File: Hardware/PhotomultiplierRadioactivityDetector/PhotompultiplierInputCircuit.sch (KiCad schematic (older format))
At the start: 40 parts, among them J10 Conn_01x01_Male, J11 Conn_01x01_Male, J12 Conn_01x01_Male, J13 Conn_01x01_Male, J14 Conn_01x01_Male, J3 Conn_01x01_Male, J4 Conn_01x01_Male, J5 Conn_01x01_Male, J6 Conn_01x01_Male, J7 Conn_01x01_Male, J8 Conn_01x01_Male, J9 Conn_01x01_Male

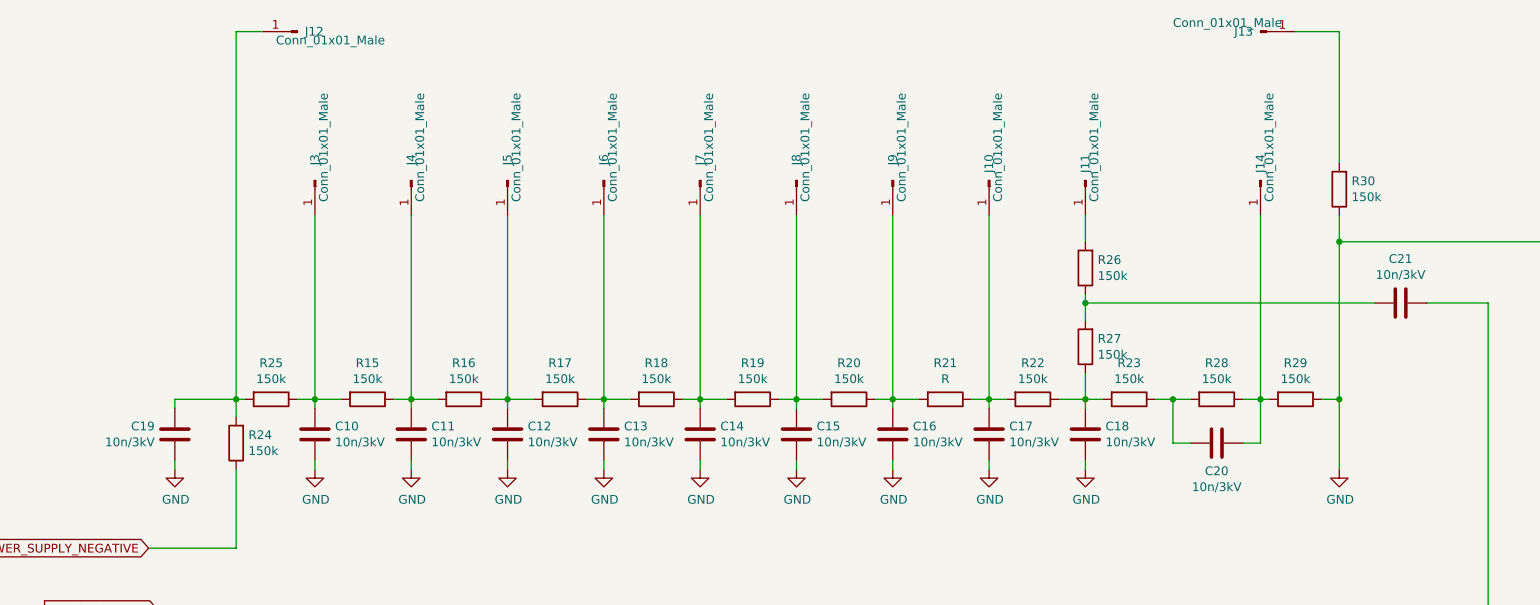
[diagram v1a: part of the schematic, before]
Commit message: draft of hw power supply
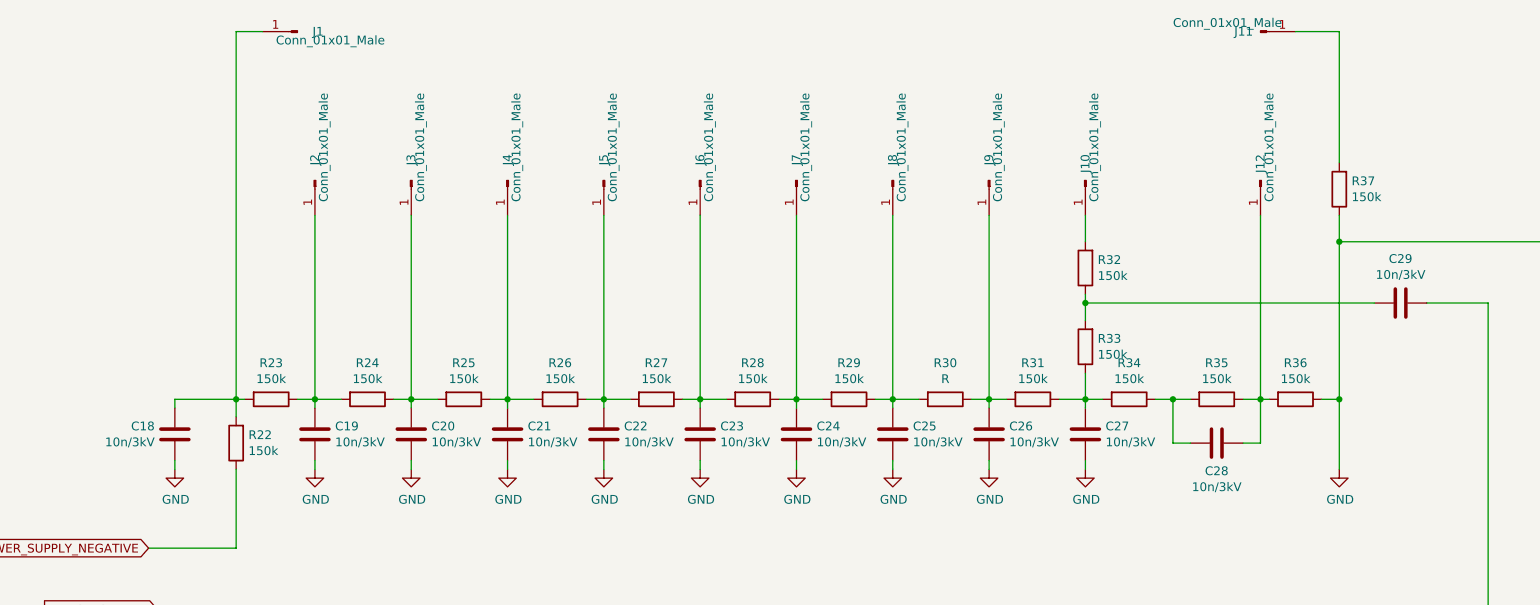
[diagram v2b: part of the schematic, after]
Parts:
- renumbered C19 to C18, C10 to C19, C11 to C20, C12 to C21, C13 to C22, C14 to C23, C15 to C24, C16 to C25, C17 to C26, C18 to C27, C20 to C28, C21 to C29, J12 to J1, J11 to J10, J13 to J11, J14 to J12, J3 to J2, J4 to J3, J5 to J4, J6 to J5, J7 to J6, J8 to J7, J9 to J8, J10 to J9, R24 to R22, R25 to R23, R15 to R24, R16 to R25, R17 to R26, R18 to R27, R19 to R28, R20 to R29, R21 to R30, R22 to R31, R26 to R32, R27 to R33, R23 to R34, R28 to R35, R29 to R36, R30 to R37

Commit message: add element/footprint for photomultiplier
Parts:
- removed J1, J10, J11, J12, J2, J3, J4, J5, J6, J7, J8, J9: Conn_01x01_Male, Connector_Pin:Pin_D1.1mm_L10.2mm_W3.5mm_Flat, symbol Connector:Conn_01x01_Male
- added EL1: Photomultiplier, PhotomultiplierRadioactivityDetector:PhotomultiplierGeneric, symbol PhotomultiplierRadioactivityDetector:Photomultiplier
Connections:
- net at C19.1, R23.1, R24.2: now also EL1.2
- net at C18.1, R22.2, R23.2: now also EL1.1
- net at C28.1, R35.1, R36.2: now also EL1.11
- net at R37.2: now also EL1.12
- net at R32.2: now also EL1.10
- net at C20.1, R24.1, R25.2: now also EL1.3
- net at C21.1, R25.1, R26.2: now also EL1.4
- net at C22.1, R26.1, R27.2: now also EL1.5
- net at C23.1, R27.1, R28.2: now also EL1.6
- net at C24.1, R28.1, R29.2: now also EL1.7
- net at C25.1, R29.1, R30.2: now also EL1.8
- net at C26.1, R30.1, R31.2: now also EL1.9
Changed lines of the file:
@@
 $EndDescr
-$Comp
-L Connector:Conn_01x01_Male J2
-U 1 1 5EDAB7C9
-P 3050 2450
-F 0 "J2" H 2900 2450 50  0000 L CNN
-F 1 "Conn_01x01_Male" H 2550 2500 50  0000 L CNN
-F 2 "Connector_Pin:Pin_D1.1mm_L10.2mm_W3.5mm_Flat" H 3050 2450 50  0001 C CNN
-F 3 "~" H 3050 2450 50  0001 C CNN
-	1    3050 2450
-	0    1    1    0
-$EndComp
 $Comp
 L Device:R R24
@@
 	3050 4100 3050 4050
 Wire Wire Line
-	3050 2650 3050 3700
-Wire Wire Line
 	3200 3700 3050 3700
 Connection ~ 3050 3700
@@
 Wire Wire Line
 	3050 3700 2950 3700
-$Comp
-L Connector:Conn_01x01_Male J3
-U 1 1 5EDAB7E7
-P 3600 2450
-F 0 "J3" H 3450 2450 50  0000 L CNN
-F 1 "Conn_01x01_Male" H 3100 2500 50  0000 L CNN
-F 2 "Connector_Pin:Pin_D1.1mm_L10.2mm_W3.5mm_Flat" H 3600 2450 50  0001 C CNN
-F 3 "~" H 3600 2450 50  0001 C CNN
-	1    3600 2450
-	0    1    1    0
-$EndComp
 $Comp
 L Device:R R25
@@
 	3600 4100 3600 4050
 Wire Wire Line
-	3600 2650 3600 3700
-Wire Wire Line
 	3750 3700 3600 3700
 Connection ~ 3600 3700
@@
 Wire Wire Line
 	3600 3700 3500 3700
-$Comp
-L Connector:Conn_01x01_Male J4
-U 1 1 5EDAB805
-P 4150 2450
-F 0 "J4" H 4000 2450 50  0000 L CNN
-F 1 "Conn_01x01_Male" H 3650 2500 50  0000 L CNN
-F 2 "Connector_Pin:Pin_D1.1mm_L10.2mm_W3.5mm_Flat" H 4150 2450 50  0001 C CNN
-F 3 "~" H 4150 2450 50  0001 C CNN
-	1    4150 2450
-	0    1    1    0
-$EndComp
 $Comp
 L Device:R R26
@@
 	4150 4100 4150 4050
 Wire Wire Line
-	4150 2650 4150 3700
-Wire Wire Line
 	4300 3700 4150 3700
 Connection ~ 4150 3700
@@
 Wire Wire Line
 	4150 3700 4050 3700
-$Comp
-L Connector:Conn_01x01_Male J5
-U 1 1 5EDAB823
-P 4700 2450
-F 0 "J5" H 4550 2450 50  0000 L CNN
-F 1 "Conn_01x01_Male" H 4200 2500 50  0000 L CNN
-F 2 "Connector_Pin:Pin_D1.1mm_L10.2mm_W3.5mm_Flat" H 4700 2450 50  0001 C CNN
-F 3 "~" H 4700 2450 50  0001 C CNN
-	1    4700 2450
-	0    1    1    0
-$EndComp
 $Comp
 L Device:R R27
@@
 	4700 4100 4700 4050
 Wire Wire Line
-	4700 2650 4700 3700
-Wire Wire Line
 	4850 3700 4700 3700
 Connection ~ 4700 3700
@@
 Wire Wire Line
 	4700 3700 4600 3700
-$Comp
-L Connector:Conn_01x01_Male J6
-U 1 1 5EDAB841
-P 5250 2450
-F 0 "J6" H 5100 2450 50  0000 L CNN
-F 1 "Conn_01x01_Male" H 4750 2500 50  0000 L CNN
-F 2 "Connector_Pin:Pin_D1.1mm_L10.2mm_W3.5mm_Flat" H 5250 2450 50  0001 C CNN
-F 3 "~" H 5250 2450 50  0001 C CNN
-	1    5250 2450
-	0    1    1    0
-$EndComp
 $Comp
 L Device:R R28
@@
 	5250 3700 5150 3700
 $Comp
-L Connector:Conn_01x01_Male J7
-U 1 1 5EDAB85F
-P 5800 2450
-F 0 "J7" H 5650 2450 50  0000 L CNN
-F 1 "Conn_01x01_Male" H 5300 2500 50  0000 L CNN
-F 2 "Connector_Pin:Pin_D1.1mm_L10.2mm_W3.5mm_Flat" H 5800 2450 50  0001 C CNN
-F 3 "~" H 5800 2450 50  0001 C CNN
-	1    5800 2450
-	0    1    1    0
-$EndComp
-$Comp
 L Device:R R29
 U 1 1 5EDAB865
@@
 	5800 3700 5700 3700
 $Comp
-L Connector:Conn_01x01_Male J8
-U 1 1 5EDAB87D
-P 6350 2450
-F 0 "J8" H 6200 2450 50  0000 L CNN
-F 1 "Conn_01x01_Male" H 5850 2500 50  0000 L CNN
-F 2 "Connector_Pin:Pin_D1.1mm_L10.2mm_W3.5mm_Flat" H 6350 2450 50  0001 C CNN
-F 3 "~" H 6350 2450 50  0001 C CNN
-	1    6350 2450
-	0    1    1    0
-$EndComp
-$Comp
 L Device:R R30
 U 1 1 5EDAB883
@@
 	6350 4100 6350 4050
 Wire Wire Line
-	6350 2650 6350 3700
-Wire Wire Line
 	6500 3700 6350 3700
 Connection ~ 6350 3700
@@
 Wire Wire Line
 	6350 3700 6250 3700
-$Comp
-L Connector:Conn_01x01_Male J9
-U 1 1 5EDAB89B
-P 6900 2450
-F 0 "J9" H 6750 2450 50  0000 L CNN
-F 1 "Conn_01x01_Male" H 6400 2500 50  0000 L CNN
-F 2 "Connector_Pin:Pin_D1.1mm_L10.2mm_W3.5mm_Flat" H 6900 2450 50  0001 C CNN
-F 3 "~" H 6900 2450 50  0001 C CNN
-	1    6900 2450
-	0    1    1    0
-$EndComp
 $Comp
 L Device:R R31
@@
 	6900 4100 6900 4050
 Wire Wire Line
-	6900 2650 6900 3700
-Wire Wire Line
 	7000 3700 6900 3700
 Connection ~ 6900 3700
@@
 Wire Wire Line
 	6900 3700 6800 3700
-$Comp
-L Connector:Conn_01x01_Male J10
-U 1 1 5EDAB8B9
-P 7450 2450
-F 0 "J10" H 7300 2450 50  0000 L CNN
-F 1 "Conn_01x01_Male" H 6950 2500 50  0000 L CNN
-F 2 "Connector_Pin:Pin_D1.1mm_L10.2mm_W3.5mm_Flat" H 7450 2450 50  0001 C CNN
-F 3 "~" H 7450 2450 50  0001 C CNN
-	1    7450 2450
-	0    1    1    0
-$EndComp
 $Comp
 L Device:R R34
@@
 Text GLabel 2100 4550 0    50   Input ~ 0
 TUBE_POWER_SUPPLY_NEGATIVE
-Wire Wire Line
-	2600 3700 2600 1600
-Wire Wire Line
-	2600 1600 2750 1600
-$Comp
-L Connector:Conn_01x01_Male J1
-U 1 1 5ED7B685
-P 2950 1600
-F 0 "J1" H 2800 1600 50  0000 L CNN
-F 1 "Conn_01x01_Male" H 2450 1650 50  0000 L CNN
-F 2 "Connector_Pin:Pin_D1.1mm_L10.2mm_W3.5mm_Flat" H 2950 1600 50  0001 C CNN
-F 3 "~" H 2950 1600 50  0001 C CNN
-	1    2950 1600
-	-1   0    0    1
-$EndComp
 $Comp
 L Device:R R35
@@
 Wire Wire Line
 	8450 3700 8500 3700
-$Comp
-L Connector:Conn_01x01_Male J12
-U 1 1 5ED81517
-P 8450 2450
-F 0 "J12" H 8300 2450 50  0000 L CNN
-F 1 "Conn_01x01_Male" H 7950 2500 50  0000 L CNN
-F 2 "Connector_Pin:Pin_D1.1mm_L10.2mm_W3.5mm_Flat" H 8450 2450 50  0001 C CNN
-F 3 "~" H 8450 2450 50  0001 C CNN
-	1    8450 2450
-	0    1    1    0
-$EndComp
-Wire Wire Line
-	8450 2650 8450 3700
 Wire Bus Line
 	11200 2550 11200 2600
-$Comp
-L Connector:Conn_01x01_Male J11
-U 1 1 5ED82C8D
-P 8450 1600
-F 0 "J11" H 8300 1600 50  0000 L CNN
-F 1 "Conn_01x01_Male" H 7950 1650 50  0000 L CNN
-F 2 "Connector_Pin:Pin_D1.1mm_L10.2mm_W3.5mm_Flat" H 8450 1600 50  0001 C CNN
-F 3 "~" H 8450 1600 50  0001 C CNN
-	1    8450 1600
-	1    0    0    -1
-$EndComp
 $Comp
 L power:GND #PWR044
@@
 Wire Wire Line
 	8900 3700 8900 2800
-Wire Wire Line
-	8650 1600 8900 1600
-Wire Wire Line
-	8900 1600 8900 2350
 $Comp
 L Device:R R33
@@
 	7450 3150 7450 3100
 Wire Wire Line
-	7450 2800 7450 2650
-Wire Wire Line
 	8900 2800 10100 2800
 Wire Wire Line
@@
 	1    0    0    -1
 $EndComp
+$Comp
+L PhotomultiplierRadioactivityDetector:Photomultiplier EL1
+U 1 1 5EE61F2A
+P 5450 1300
+F 0 "EL1" H 5525 1615 50  0000 C CNN
+F 1 "Photomultiplier" H 5525 1524 50  0000 C CNN
+F 2 "PhotomultiplierRadioactivityDetector:PhotomultiplierGeneric" H 5450 1550 50  0001 C CNN
+F 3 "" H 5450 1550 50  0001 C CNN
+	1    5450 1300
+	1    0    0    -1
+$EndComp
+Wire Wire Line
+	3050 1900 4850 1900
+Wire Wire Line
+	4850 1900 4850 1550
+Wire Wire Line
+	3050 1900 3050 3700
+Wire Wire Line
+	3600 2100 5000 2100
+Wire Wire Line
+	5000 2100 5000 1550
+Wire Wire Line
+	3600 2100 3600 3700
+Wire Wire Line
+	4150 2250 5150 2250
+Wire Wire Line
+	5150 2250 5150 1550
+Wire Wire Line
+	4150 2250 4150 3700
+Wire Wire Line
+	4700 2400 5300 2400
+Wire Wire Line
+	5300 2400 5300 1550
+Wire Wire Line
+	4700 2400 4700 3700
+Wire Wire Line
+	5450 2650 5450 1550
+Wire Wire Line
+	5250 2650 5450 2650
+Wire Wire Line
+	5600 2650 5600 1550
+Wire Wire Line
+	5600 2650 5800 2650
+Wire Wire Line
+	6350 2400 5750 2400
+Wire Wire Line
+	5750 2400 5750 1550
+Wire Wire Line
+	6350 2400 6350 3700
+Wire Wire Line
+	6900 2200 5900 2200
+Wire Wire Line
+	5900 2200 5900 1550
+Wire Wire Line
+	6900 2200 6900 3700
+Wire Wire Line
+	7450 2050 6050 2050
+Wire Wire Line
+	6050 2050 6050 1550
+Wire Wire Line
+	7450 2050 7450 2800
+Wire Wire Line
+	8450 1850 6200 1850
+Wire Wire Line
+	6200 1850 6200 1550
+Wire Wire Line
+	8450 1850 8450 3700
+Wire Wire Line
+	2600 1300 4600 1300
+Wire Wire Line
+	6450 1300 8900 1300
+Wire Wire Line
+	2600 1300 2600 3700
+Wire Wire Line
+	8900 1300 8900 2350
 $EndSCHEMATC

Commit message: draft of amplifier
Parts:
- added C33, C34: 10n/3kV, Capacitor_THT:C_Disc_D11.0mm_W5.0mm_P7.50mm, symbol Device:C
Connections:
- net DYNOE_OUTPUT: now also C20.2, R33.1; no longer C29.1
- net GND: now also C18.1, C25.1, EL1.12, R32.2, R33.2, C34.1; no longer C18.2, C19.2, C20.2, C21.2, C22.2, C23.2, C24.2, C25.2, C26.2, C27.2, R36.1
- net at EL1.2, R23.1, R24.2: now also C26.1, C27.2, R35.1; no longer C19.1
- net at EL1.1, R22.2, R23.2: now also C18.2, C21.2, C26.2, R34.1; no longer C18.1
- net at R37.2: now also EL1.11, R36.1; no longer EL1.12
- net at EL1.10: now also R31.1, R36.2, C33.1, C34.2; no longer R32.2
- net at EL1.3, R24.1, R25.2: now also C21.1, C22.2; no longer C20.1
- net at EL1.4, R25.1, R26.2: now also C27.1, C28.2; no longer C21.1
- net at C22.1, EL1.5, R26.1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: now also C23.2
- net at EL1.6, R27.1, R28.2: now also C28.1, C29.2; no longer C23.1
- net at EL1.7, R28.1, R29.2: now also C23.1, C24.2; no longer C24.1
- net at EL1.8, R29.1, R30.2: now also C29.1, C33.2; no longer C25.1
- net at EL1.9, R30.1, R31.2: now also C24.1, C25.2; no longer C26.1
- new net: C19.1, R34.2
- new net: C20.1, R35.2
- new net ANODE_OUTPUT: C19.2, R32.1
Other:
- moved on the sheet: C18, EL1, R22, R23, R24, R25, R26, R27, R28, R29, R30, R31

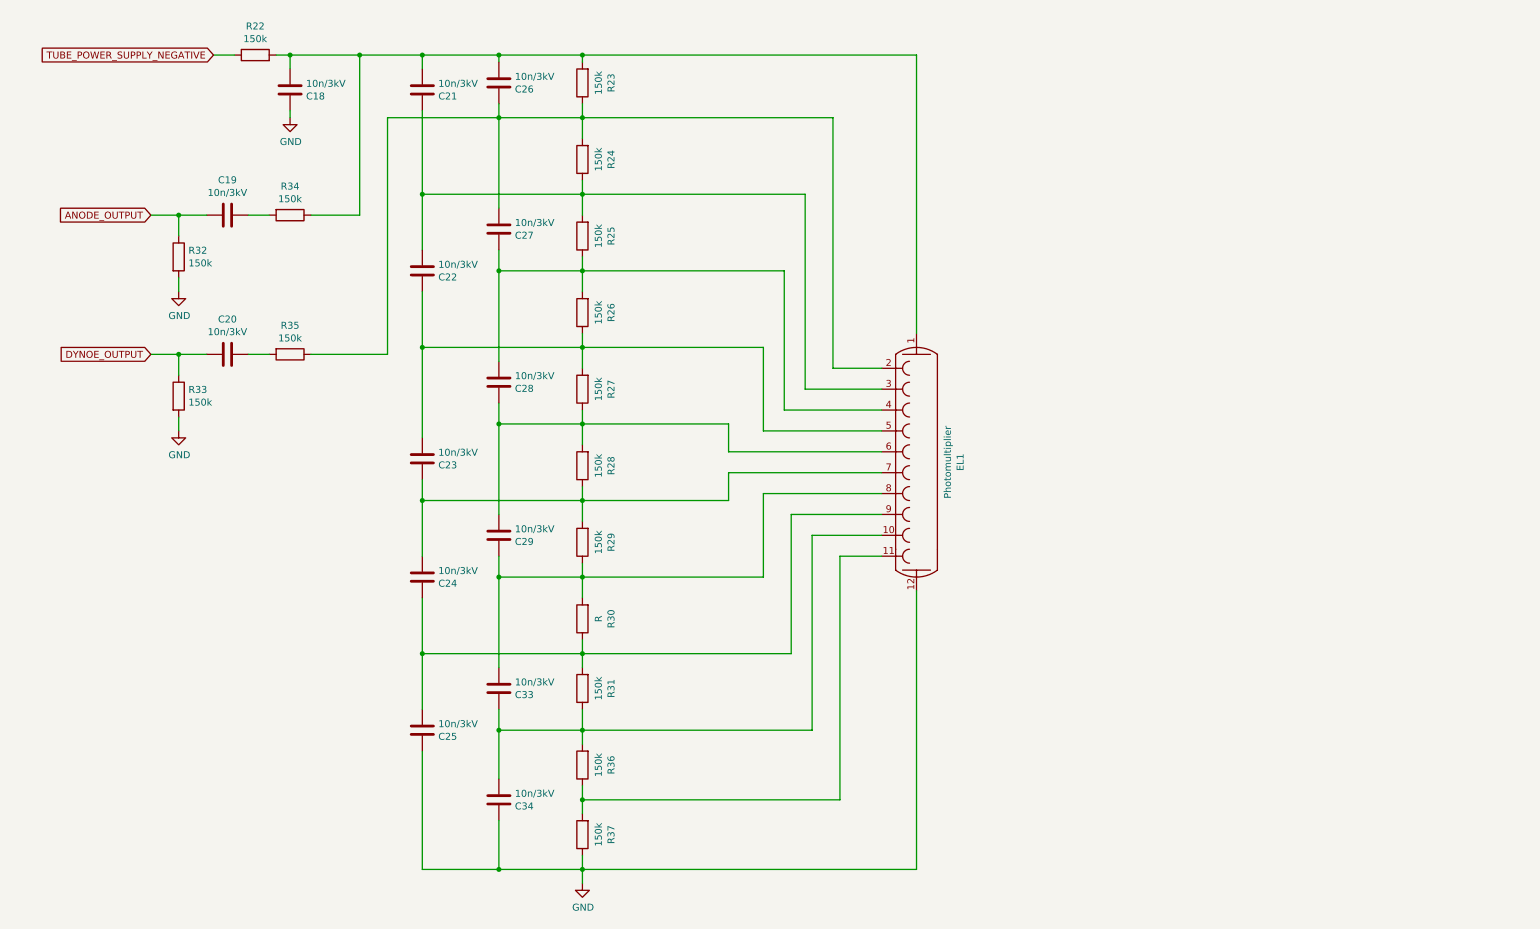
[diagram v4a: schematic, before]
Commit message: reworked power supply for tube
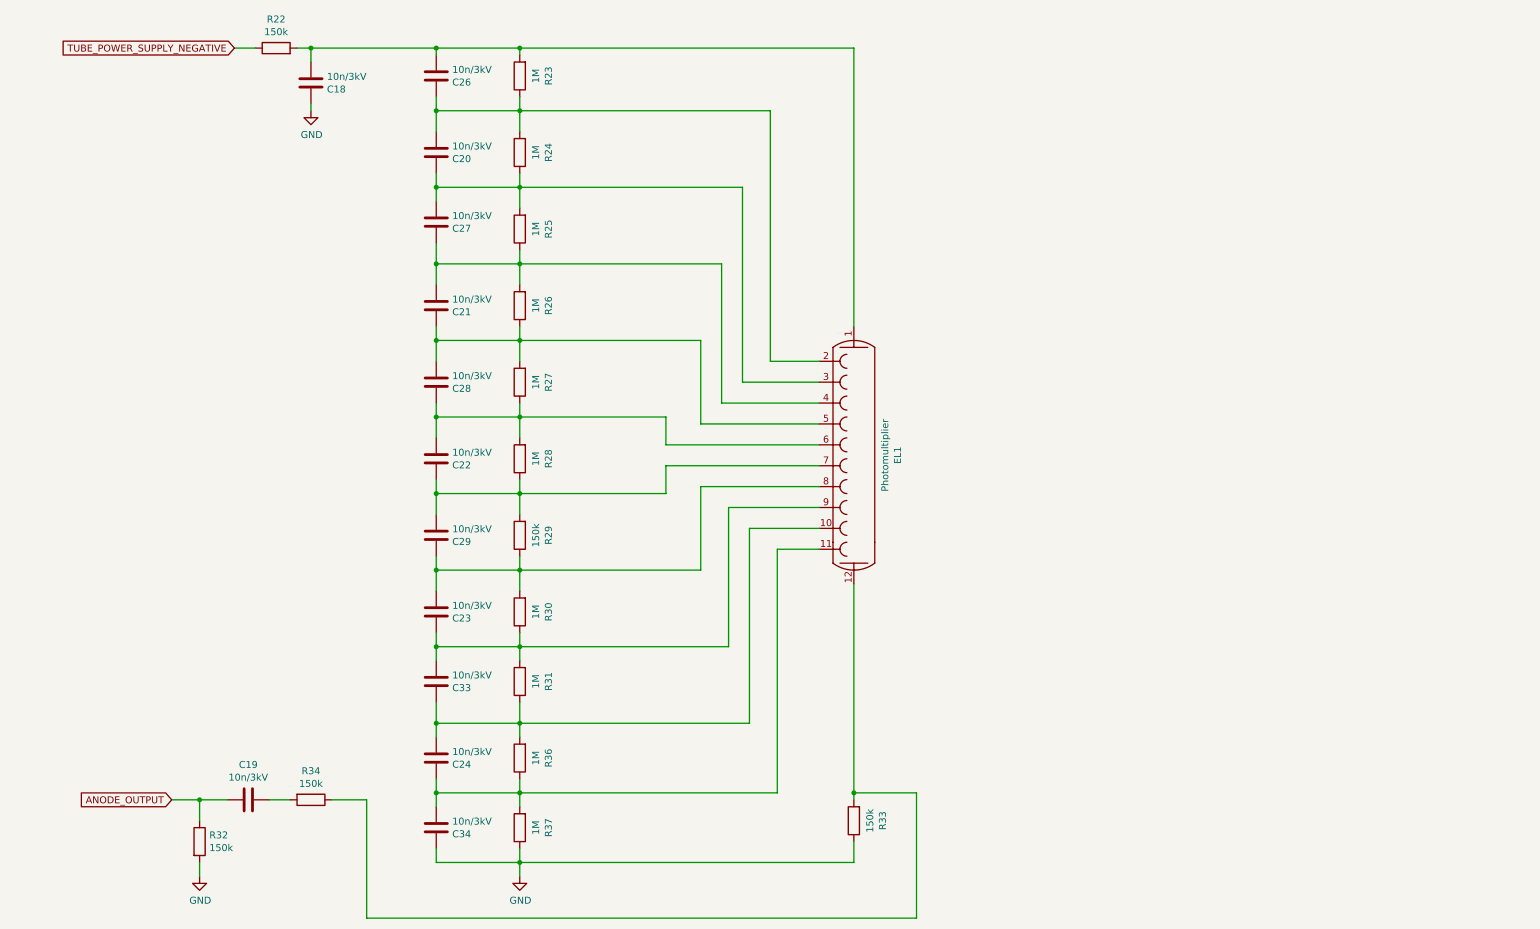
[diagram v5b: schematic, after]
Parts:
- removed C25: 10n/3kV, Capacitor_THT:C_Disc_D11.0mm_W5.0mm_P7.50mm, symbol Device:C
- removed R35: 150k, Resistor_THT:R_Axial_DIN0411_L9.9mm_D3.6mm_P12.70mm_Horizontal, symbol Device:R
- C20, C21, C22, C23, C24, C26, C27, C28, C29, C33, C34: footprint Capacitor_THT:C_Disc_D11.0mm_W5.0mm_P7.50mm -> Capacitor_SMD:C_1206_3216Metric
- R23, R24, R25, R26, R27, R28, R31, R36, R37: value 150k -> 1M; footprint Resistor_THT:R_Axial_DIN0411_L9.9mm_D3.6mm_P12.70mm_Horizontal -> Resistor_SMD:R_MELF_MMB-0207
- R29: footprint Resistor_THT:R_Axial_DIN0411_L9.9mm_D3.6mm_P12.70mm_Horizontal -> Resistor_SMD:R_MELF_MMB-0207
- R30: value R -> 1M; footprint Resistor_THT:R_Axial_DIN0411_L9.9mm_D3.6mm_P12.70mm_Horizontal -> Resistor_SMD:R_MELF_MMB-0207
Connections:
- net GND: now also R33.1; no longer EL1.12, R33.2
- net at C26.1, EL1.2, R23.1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: now also C20.2; no longer C27.2
- net at C18.2, C26.2, EL1.1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: no longer C21.2, R34.1
- net at EL1.3, R24.1, R25.2: now also C20.1, C27.2; no longer C21.1, C22.2
- net at C27.1, EL1.4, R25.1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: now also C21.2; no longer C28.2
- net at EL1.5, R26.1, R27.2: now also C21.1, C28.2; no longer C22.1, C23.2
- net at C28.1, EL1.6, R27.1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: now also C22.2; no longer C29.2
- net at EL1.7, R28.1, R29.2: now also C22.1, C29.2; no longer C23.1, C24.2
- net at C29.1, EL1.8, R29.1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: now also C23.2; no longer C33.2
- net at EL1.9, R30.1, R31.2: now also C23.1, C33.2; no longer C24.1
- net at C33.1, EL1.10, R31.1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: now also C24.2; no longer C34.2
- net at EL1.11, R36.1, R37.2: now also C24.1, C34.2
- removed net DYNOE_OUTPUT: C20.2, R33.1
- new net: EL1.12, R33.2, R34.1
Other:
- moved on the sheet: C18, C19, C26, C27, C28, C29, C33, C34, EL1, R22, R23, R24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
